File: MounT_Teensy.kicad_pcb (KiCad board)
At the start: 2 copper layers, 61.2 x 18 mm, 10 parts, among them J1 Teensy, J2 DB25_Male, U1 MAX3232

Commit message: remove unused models, update readme
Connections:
- net /CTS renamed /CTS_232
- net /DCD renamed /DCD_232
- net /DSR renamed /DSR_232
- net /DTR renamed /DTR_232
- net /RTS renamed /RTS_232
- net /RXD renamed /RX_232
- net /RXD_TTL renamed /RX_TTL
- net /TXD renamed /TX_232
- net /TXD_TTL renamed /TX_TTL
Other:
- board text added: "SD CARD"
- board text added: "USB"

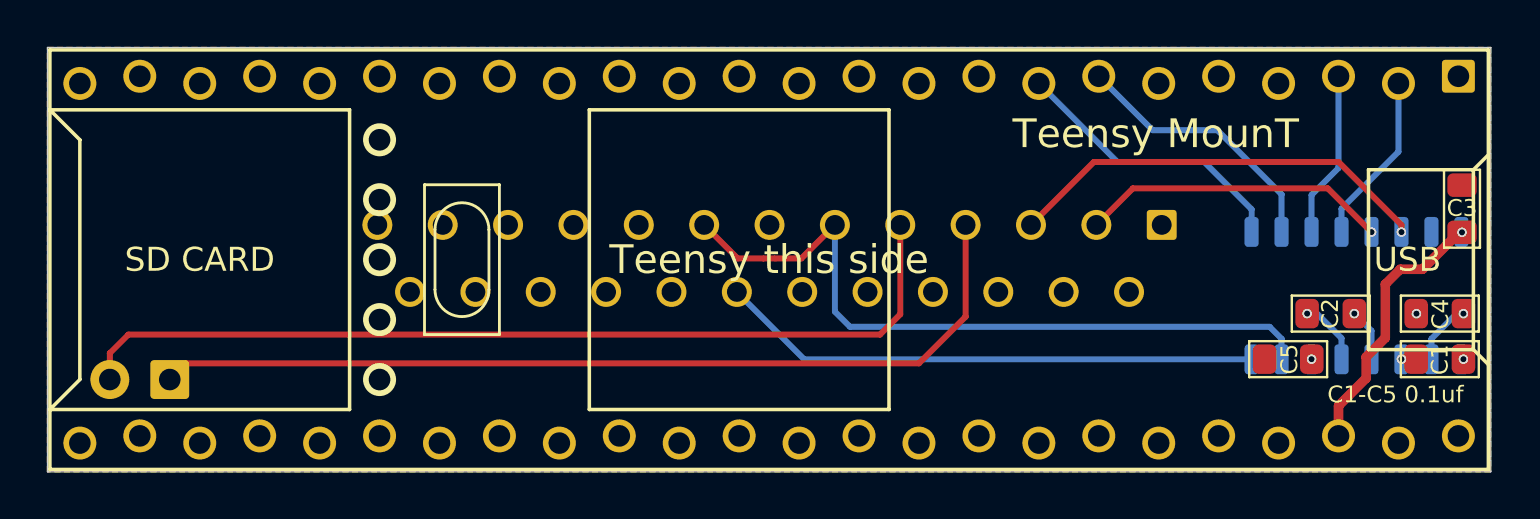
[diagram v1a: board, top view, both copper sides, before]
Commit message: reduce pin stagger offset from 12 mils to 8 mils
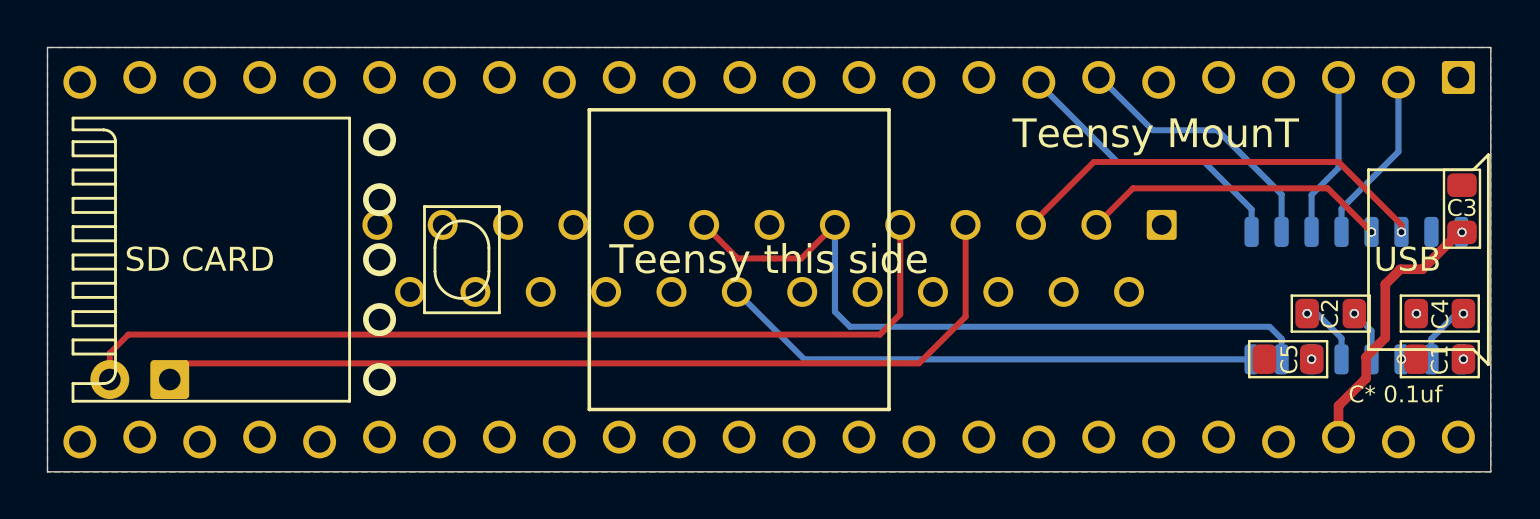
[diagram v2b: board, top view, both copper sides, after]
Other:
- board text added: "C* 0.1uf"
- board text removed: "C1-C5 0.1uf"

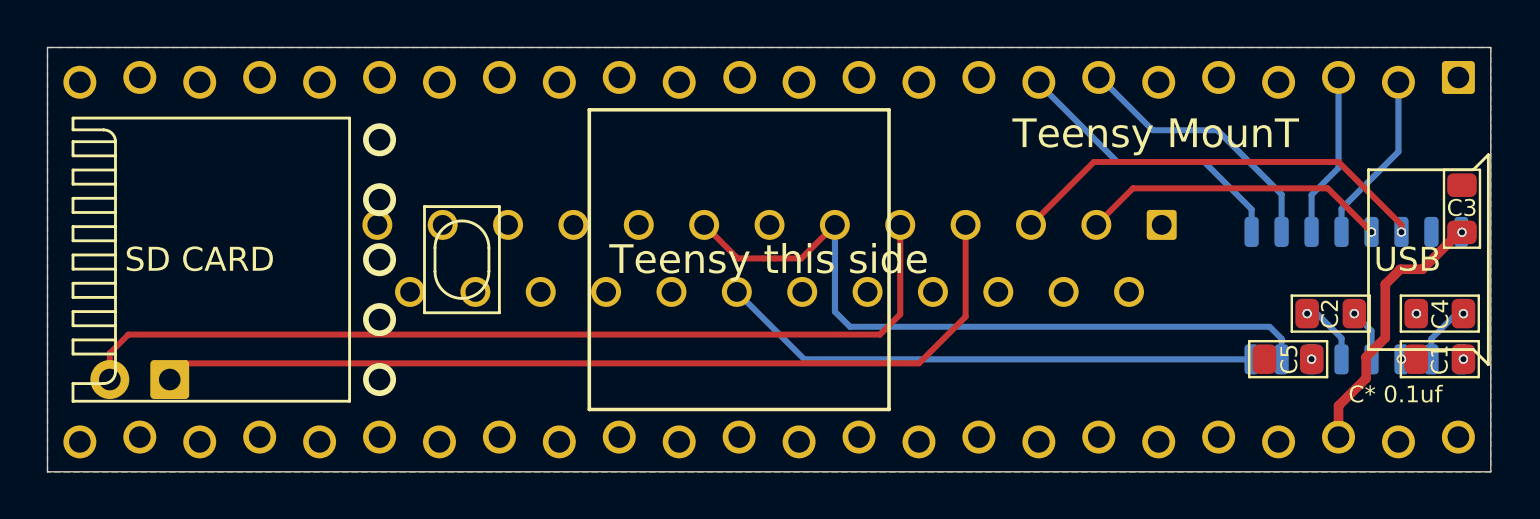
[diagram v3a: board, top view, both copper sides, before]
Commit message: reduce pin stagger offset to 4mil
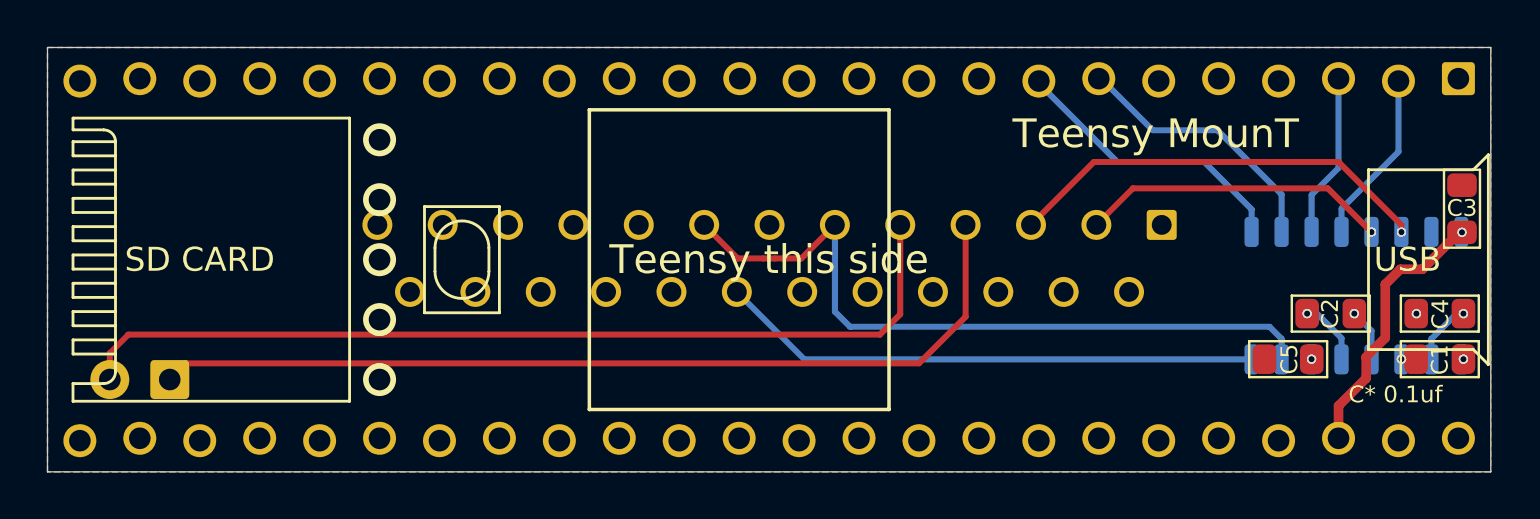
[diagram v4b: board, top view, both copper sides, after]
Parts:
- J1: footprint 0_LOCAL:Teensy_MounT_stagger -> 0_LOCAL:Teensy_MounT_stagger_4mil

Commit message: use 6mil stagger, 4mil wasn't good enough
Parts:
- J1: footprint 0_LOCAL:Teensy_MounT_stagger_4mil -> 0_LOCAL:Teensy_MounT_stagger_6mil
